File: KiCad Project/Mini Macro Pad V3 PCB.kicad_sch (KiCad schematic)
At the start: 98 parts, among them J1 USB_C_Receptacle_USB2.0_14P, SW1 SW_Push bootsel, SW10 SW_Push, SW11 SW_Push, SW12 SW_Push, SW13 SW_Push, SW14 SW_Push, SW15 SW_Push, SW16 SW_Push, SW17 SW_Push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

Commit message: more routing traces.
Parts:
- added R7: DNF, Resistor_SMD:R_0402_1005Metric_Pad0.72x0.64mm_HandSolder, symbol Device:R_Small
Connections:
- net +3.3V: now also R7.2; no longer R1.2, U1.56 (QSPI_SS), U3.1 (~{CS})
- new net QSPI_SS: R1.2, R7.1, U1.56 (QSPI_SS), U3.1 (~{CS})
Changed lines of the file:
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@@
 	)
 	(junction
-		(at 57.15 151.13)
+		(at 35.56 113.03)
 		(diameter 0)
 		(color 0 0 0 0)
 	)
 	(junction
-		(at 252.73 50.8)
+		(at 57.15 151.13)
 		(diameter 0)
 		(color 0 0 0 0)
 	)
 	(junction
-		(at 96.52 185.42)
+		(at 252.73 50.8)
 		(diameter 0)
 		(color 0 0 0 0)
 	)
 	(junction
-		(at 132.08 156.21)
+		(at 96.52 185.42)
 		(diameter 0)
 		(color 0 0 0 0)
 	)
 	(junction
-		(at 58.42 106.68)
+		(at 132.08 156.21)
 		(diameter 0)
 		(color 0 0 0 0)
@@
 	)
 	(junction
-		(at 35.56 19.05)
+		(at 58.42 104.14)
 		(diameter 0)
 		(color 0 0 0 0)
 	)
 	(junction
-		(at 35.56 113.03)
+		(at 35.56 19.05)
 		(diameter 0)
 		(color 0 0 0 0)
@@
 	(wire
 		(pts
+			(xy 35.56 104.14) (xy 35.56 113.03)
+		)
+		(stroke
+			(width 0)
+			(type default)
+		)
+	)
+	(wire
+		(pts
 			(xy 144.78 186.69) (xy 144.78 187.96)
 		)
@@
 	(wire
 		(pts
+			(xy 55.88 104.14) (xy 58.42 104.14)
+		)
+		(stroke
+			(width 0)
+			(type default)
+		)
+	)
+	(wire
+		(pts
 			(xy 196.85 54.61) (xy 203.2 54.61)
 		)
@@
 	(wire
 		(pts
+			(xy 35.56 113.03) (xy 48.26 113.03)
+		)
+		(stroke
+			(width 0)
+			(type default)
+		)
+	)
+	(wire
+		(pts
 			(xy 231.14 96.52) (xy 232.41 96.52)
 		)
@@
 	(wire
 		(pts
-			(xy 135.89 175.26) (xy 134.62 175.26)
-		)
-		(stroke
-			(width 0)
-			(type default)
-		)
-	)
-	(wire
-		(pts
 			(xy 231.14 73.66) (xy 246.38 73.66)
 		)
@@
 	(wire
 		(pts
-			(xy 35.56 106.68) (xy 35.56 113.03)
-		)
-		(stroke
-			(width 0)
-			(type default)
-		)
-	)
-	(wire
-		(pts
 			(xy 121.92 185.42) (xy 121.92 195.58)
 		)
@@
 	(wire
 		(pts
-			(xy 58.42 96.52) (xy 58.42 106.68)
+			(xy 58.42 96.52) (xy 58.42 104.14)
 		)
 		(stroke
@@
 	(wire
 		(pts
-			(xy 35.56 113.03) (xy 48.26 113.03)
-		)
-		(stroke
-			(width 0)
-			(type default)
-		)
-	)
-	(wire
-		(pts
 			(xy 231.14 119.38) (xy 232.41 119.38)
 		)
@@
 	(wire
 		(pts
-			(xy 97.79 185.42) (xy 96.52 185.42)
-		)
-		(stroke
-			(width 0)
-			(type default)
-		)
-	)
-	(wire
-		(pts
 			(xy 109.22 165.1) (xy 109.22 175.26)
 		)
@@
 	(wire
 		(pts
-			(xy 35.56 106.68) (xy 58.42 106.68)
+			(xy 35.56 104.14) (xy 50.8 104.14)
 		)
 		(stroke
@@
 	(wire
 		(pts
-			(xy 58.42 106.68) (xy 58.42 107.95)
+			(xy 58.42 104.14) (xy 58.42 107.95)
 		)
 		(stroke
@@
 		)
 	)
+	(label "USB_BOOTSEL"
+		(at 49.53 104.14 180)
+		(effects
+			(font
+				(size 1.27 1.27)
+			)
+			(justify right bottom)
+		)
+	)
 	(label "MATRIX_R1"
 		(at 156.21 156.21 180)
@@
 					(unit 1)
 				)
+			)
+		)
+	)
+	(symbol
+		(lib_id "Device:R_Small")
+		(at 53.34 104.14 90)
+		(unit 1)
+		(exclude_from_sim yes)
+		(in_bom no)
+		(on_board no)
+		(dnp yes)
+		(fields_autoplaced yes)
+		(property "Reference" "R7"
+			(at 53.34 99.06 90)
+			(effects
+				(font
+					(size 1.016 1.016)
+				)
+			)
+		)
+		(property "Value" "DNF"
+			(at 53.34 101.6 90)
+			(effects
+				(font
+					(size 1.27 1.27)
+				)
+			)
+		)
+		(property "Footprint" "Resistor_SMD:R_0402_1005Metric_Pad0.72x0.64mm_HandSolder"
+			(at 53.34 104.14 0)
+			(effects
+				(font
+					(size 1.27 1.27)
+				)
+				(hide yes)
+			)
+		)
+		(property "Datasheet" "~"
+			(at 53.34 104.14 0)
+			(effects
+				(font
+					(size 1.27 1.27)
+				)
+				(hide yes)
+			)
+		)
+		(property "Description" "Resistor, small symbol"
+			(at 53.34 104.14 0)
+			(effects
+				(font
+					(size 1.27 1.27)
+				)
+				(hide yes)
+			)
+		)
+		(pin "1"
+		)
+		(pin "2"
+		)
+		(instances
+			(project "Mini Macro Pad V3 PCB"
+				(path "/2a066f6e-231b-48de-a223-e3e72af8ed07"
+					(reference "R7")
+					(unit 1)
+				)

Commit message: more routing work
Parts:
- removed TP10, TP11, TP12, TP7, TP8, TP9: ~, TestPoint:TestPoint_Pad_1.5x1.5mm, symbol Connector:TestPoint
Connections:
- net +3.3V: now also U1.26 (RUN)
- no-connect marks 2 -> 7

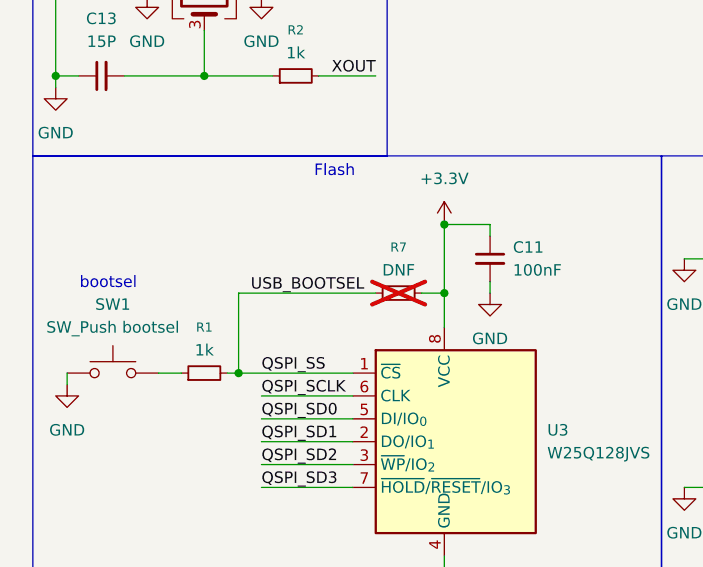
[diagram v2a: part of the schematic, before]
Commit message: tweaks for DRC
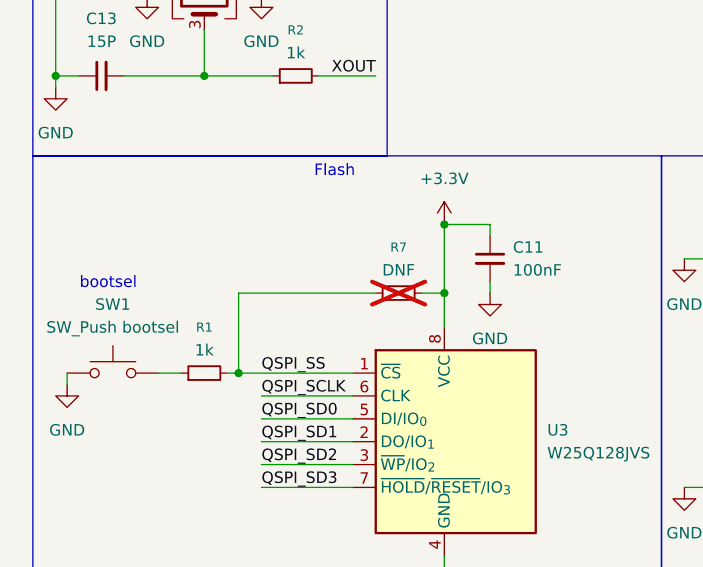
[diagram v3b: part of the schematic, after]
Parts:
- U1: footprint Package_DFN_QFN:QFN-56-1EP_7x7mm_P0.4mm_EP3.2x3.2mm -> Package_DFN_QFN:QFN-56-1EP_7x7mm_P0.4mm_EP3.2x3.2mm_ThermalVias
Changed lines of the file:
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@@
 		)
 	)
-	(label "USB_BOOTSEL"
-		(at 49.53 104.14 180)
-		(effects
-			(font
-				(size 1.27 1.27)
-			)
-			(justify right bottom)
-		)
-	)
 	(label "MATRIX_R1"
 		(at 156.21 156.21 180)
@@
 			)
 		)
-		(property "Footprint" "Package_DFN_QFN:QFN-56-1EP_7x7mm_P0.4mm_EP3.2x3.2mm"
+		(property "Footprint" "Package_DFN_QFN:QFN-56-1EP_7x7mm_P0.4mm_EP3.2x3.2mm_ThermalVias"
 			(at 205.74 109.22 0)
 			(effects

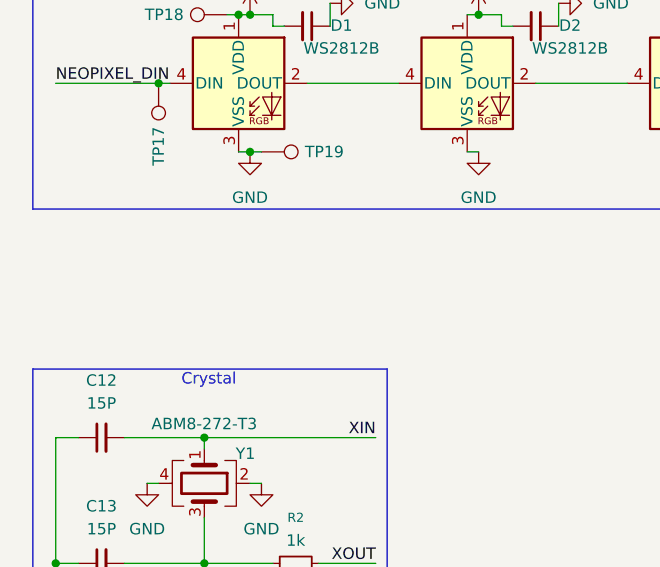
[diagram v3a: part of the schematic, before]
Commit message: added silkscreen things
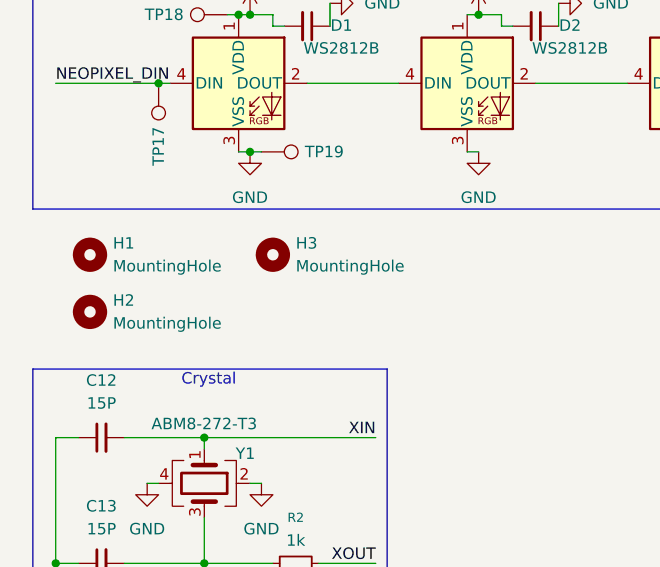
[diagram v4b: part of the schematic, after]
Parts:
- added H1, H2, H3: MountingHole, MountingHole:ToolingHole_1.152mm, symbol Mechanical:MountingHole
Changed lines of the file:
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@@
 	)
 	(symbol
+		(lib_id "Mechanical:MountingHole")
+		(at 39.37 45.72 0)
+		(unit 1)
+		(exclude_from_sim no)
+		(in_bom no)
+		(on_board yes)
+		(dnp no)
+		(fields_autoplaced yes)
+		(property "Reference" "H3"
+			(at 41.91 44.4499 0)
+			(effects
+				(font
+					(size 1.27 1.27)
+				)
+				(justify left)
+			)
+		)
+		(property "Value" "MountingHole"
+			(at 41.91 46.9899 0)
+			(effects
+				(font
+					(size 1.27 1.27)
+				)
+				(justify left)
+			)
+		)
+		(property "Footprint" "MountingHole:ToolingHole_1.152mm"
+			(at 39.37 45.72 0)
+			(effects
+				(font
+					(size 1.27 1.27)
+				)
+				(hide yes)
+			)
+		)
+		(property "Datasheet" "~"
+			(at 39.37 45.72 0)
+			(effects
+				(font
+					(size 1.27 1.27)
+				)
+				(hide yes)
+			)
+		)
+		(property "Description" "Mounting Hole without connection"
+			(at 39.37 45.72 0)
+			(effects
+				(font
+					(size 1.27 1.27)
+				)
+				(hide yes)
+			)
+		)
+		(instances
+			(project ""
+				(path "/2a066f6e-231b-48de-a223-e3e72af8ed07"
+					(reference "H3")
+					(unit 1)
+				)
+			)
+		)
+	)
+	(symbol
 		(lib_id "Device:C")
 		(at 83.82 156.21 0)
@@
 					(unit 1)
 				)
+			)
+		)
+	)
+	(symbol
+		(lib_id "Mechanical:MountingHole")
+		(at 19.05 45.72 0)
+		(unit 1)
+		(exclude_from_sim no)
+		(in_bom no)
+		(on_board yes)
+		(dnp no)
+		(fields_autoplaced yes)
+		(property "Reference" "H1"
+			(at 21.59 44.4499 0)
+			(effects
+				(font
+					(size 1.27 1.27)
+				)
+				(justify left)
+			)
+		)
+		(property "Value" "MountingHole"
+			(at 21.59 46.9899 0)
+			(effects
+				(font
+					(size 1.27 1.27)
+				)
+				(justify left)
+			)
+		)
+		(property "Footprint" "MountingHole:ToolingHole_1.152mm"
+			(at 19.05 45.72 0)
+			(effects
+				(font
+					(size 1.27 1.27)
+				)
+				(hide yes)
+			)
+		)
+		(property "Datasheet" "~"
+			(at 19.05 45.72 0)
+			(effects
+				(font
+					(size 1.27 1.27)
+				)
+				(hide yes)
+			)
+		)
+		(property "Description" "Mounting Hole without connection"
+			(at 19.05 45.72 0)
+			(effects
+				(font
+					(size 1.27 1.27)
+				)
+				(hide yes)
+			)
+		)
+		(instances
+			(project ""
+				(path "/2a066f6e-231b-48de-a223-e3e72af8ed07"
+					(reference "H1")
+					(unit 1)
+				)
+			)
+		)
+	)
+	(symbol
+		(lib_id "Mechanical:MountingHole")
+		(at 19.05 52.07 0)
+		(unit 1)
+		(exclude_from_sim no)
+		(in_bom no)
+		(on_board yes)
+		(dnp no)
+		(fields_autoplaced yes)
+		(property "Reference" "H2"
+			(at 21.59 50.7999 0)
+			(effects
+				(font
+					(size 1.27 1.27)
+				)
+				(justify left)
+			)
+		)
+		(property "Value" "MountingHole"
+			(at 21.59 53.3399 0)
+			(effects
+				(font
+					(size 1.27 1.27)
+				)
+				(justify left)
+			)
+		)
+		(property "Footprint" "MountingHole:ToolingHole_1.152mm"
+			(at 19.05 52.07 0)
+			(effects
+				(font
+					(size 1.27 1.27)
+				)
+				(hide yes)
+			)
+		)
+		(property "Datasheet" "~"
+			(at 19.05 52.07 0)
+			(effects
+				(font
+					(size 1.27 1.27)
+				)
+				(hide yes)
+			)
+		)
+		(property "Description" "Mounting Hole without connection"
+			(at 19.05 52.07 0)
+			(effects
+				(font
+					(size 1.27 1.27)
+				)
+				(hide yes)
+			)
+		)
+		(instances
+			(project ""
+				(path "/2a066f6e-231b-48de-a223-e3e72af8ed07"
+					(reference "H2")
+					(unit 1)
+				)

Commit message: small tweaks before ordering first prototype
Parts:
- added TP7, TP8: ~, TestPoint:TestPoint_Pad_1.5x1.5mm, symbol Connector:TestPoint
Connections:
- net USB_D+: now also TP8.1
- net USB_D-: now also TP7.1
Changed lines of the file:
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@@
+	)
+	(symbol
+		(lib_id "Connector:TestPoint")
+		(at 54.61 171.45 270)
+		(unit 1)
+		(exclude_from_sim no)
+		(in_bom yes)
+		(on_board yes)
+		(dnp no)
+		(property "Reference" "TP8"
+			(at 59.436 171.45 90)
+			(effects
+				(font
+					(size 1.27 1.27)
+				)
+				(justify left)
+			)
+		)
+		(property "Value" "~"
+			(at 59.69 172.7199 90)
+			(effects
+				(font
+					(size 1.27 1.27)
+				)
+				(justify left)
+				(hide yes)
+			)
+		)
+		(property "Footprint" "TestPoint:TestPoint_Pad_1.5x1.5mm"
+			(at 54.61 176.53 0)
+			(effects
+				(font
+					(size 1.27 1.27)
+				)
+				(hide yes)
+			)
+		)
+		(property "Datasheet" "~"
+			(at 54.61 176.53 0)
+			(effects
+				(font
+					(size 1.27 1.27)
+				)
+				(hide yes)
+			)
+		)
+		(property "Description" "test point"
+			(at 54.61 171.45 0)
+			(effects
+				(font
+					(size 1.27 1.27)
+				)
+				(hide yes)
+			)
+		)
+		(pin "1"
+		)
+		(instances
+			(project "Mini Macro Pad V3 PCB"
+				(path "/2a066f6e-231b-48de-a223-e3e72af8ed07"
+					(reference "TP8")
+					(unit 1)
+				)
+			)
+		)
 	)
 	(symbol
@@
 					(unit 1)
 				)
+			)
+		)
+	)
+	(symbol
+		(lib_id "Connector:TestPoint")
+		(at 54.61 167.64 270)
+		(unit 1)
+		(exclude_from_sim no)
+		(in_bom yes)
+		(on_board yes)
+		(dnp no)
+		(property "Reference" "TP7"
+			(at 59.436 167.64 90)
+			(effects
+				(font
+					(size 1.27 1.27)
+				)
+				(justify left)
+			)
+		)
+		(property "Value" "~"
+			(at 59.69 168.9099 90)
+			(effects
+				(font
+					(size 1.27 1.27)
+				)
+				(justify left)
+				(hide yes)
+			)
+		)
+		(property "Footprint" "TestPoint:TestPoint_Pad_1.5x1.5mm"
+			(at 54.61 172.72 0)
+			(effects
+				(font
+					(size 1.27 1.27)
+				)
+				(hide yes)
+			)
+		)
+		(property "Datasheet" "~"
+			(at 54.61 172.72 0)
+			(effects
+				(font
+					(size 1.27 1.27)
+				)
+				(hide yes)
+			)
+		)
+		(property "Description" "test point"
+			(at 54.61 167.64 0)
+			(effects
+				(font
+					(size 1.27 1.27)
+				)
+				(hide yes)
+			)
+		)
+		(pin "1"
+		)
+		(instances
+			(project "Mini Macro Pad V3 PCB"
+				(path "/2a066f6e-231b-48de-a223-e3e72af8ed07"
+					(reference "TP7")
+					(unit 1)
+				)

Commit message: changed capacitor & resistor sizes
changed sizes from 0402 to 0603 & replaced BOOTSEL button with the same kind as all the others
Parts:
- C1, C10, C11, C12, C13, C14, C15, C16, C17, C18, C19, C2, C20, C21, C22, C23, C3, C4, C5, C6, C7, C8, C9: footprint Capacitor_SMD:C_0402_1005Metric_Pad0.74x0.62mm_HandSolder -> Capacitor_SMD:C_0603_1608Metric
- R1, R2, R3, R4, R5, R6: footprint Resistor_SMD:R_0402_1005Metric_Pad0.72x0.64mm_HandSolder -> Resistor_SMD:R_0603_1608Metric
- SW1: footprint Button_Switch_SMD:Panasonic_EVQPUK_EVQPUB -> Button_Switch_THT:SW_PUSH_6mm_H4.3mm; LSSC (none) -> C526225
- U1: LSSC (none) -> C2040
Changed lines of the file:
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@@
 			)
 		)
-		(property "Footprint" "Capacitor_SMD:C_0402_1005Metric_Pad0.74x0.62mm_HandSolder"
+		(property "Footprint" "Capacitor_SMD:C_0603_1608Metric"
 			(at 252.73 53.34 0)
 			(effects
@@
 			)
 		)
-		(property "Footprint" "Resistor_SMD:R_0402_1005Metric_Pad0.72x0.64mm_HandSolder"
+		(property "Footprint" "Resistor_SMD:R_0603_1608Metric"
 			(at 171.45 73.66 0)
 			(effects
@@
 			)
 		)
-		(property "Footprint" "Resistor_SMD:R_0402_1005Metric_Pad0.72x0.64mm_HandSolder"
+		(property "Footprint" "Resistor_SMD:R_0603_1608Metric"
 			(at 41.91 80.01 0)
 			(effects
@@
 			)
 		)
-		(property "Footprint" "Button_Switch_SMD:Panasonic_EVQPUK_EVQPUB"
+		(property "Footprint" "Button_Switch_THT:SW_PUSH_6mm_H4.3mm"
 			(at 21.59 107.95 0)
 			(effects
@@
 			)
 		)
-		(property "Datasheet" "~"
+		(property "Datasheet" "https://jlcpcb.com/api/file/downloadByFileSystemAccessId/8588913898988298240"
 			(at 21.59 107.95 0)
 			(effects
@@
 			)
 		)
+		(property "LSSC" "C526225"
+			(at 21.59 113.03 0)
+			(effects
+				(font
+					(size 1.27 1.27)
+				)
+				(hide yes)
+			)
+		)
 		(pin "2"
 		)
@@
 			)
 		)
-		(property "Footprint" "Resistor_SMD:R_0402_1005Metric_Pad0.72x0.64mm_HandSolder"
+		(property "Footprint" "Resistor_SMD:R_0603_1608Metric"
 			(at 46.99 158.75 0)
 			(effects
@@
 			)
 		)
-		(property "Footprint" "Resistor_SMD:R_0402_1005Metric_Pad0.72x0.64mm_HandSolder"
+		(property "Footprint" "Resistor_SMD:R_0603_1608Metric"
 			(at 171.45 81.28 0)
 			(effects
@@
 			)
 		)
-		(property "Footprint" "Capacitor_SMD:C_0402_1005Metric_Pad0.74x0.62mm_HandSolder"
+		(property "Footprint" "Capacitor_SMD:C_0603_1608Metric"
 			(at 84.7852 160.02 0)
 			(effects
@@
 			)
 		)
-		(property "Footprint" "Capacitor_SMD:C_0402_1005Metric_Pad0.74x0.62mm_HandSolder"
+		(property "Footprint" "Capacitor_SMD:C_0603_1608Metric"
 			(at 275.59 53.34 0)
 			(effects
@@
 			)
 		)
-		(property "Footprint" "Resistor_SMD:R_0402_1005Metric_Pad0.72x0.64mm_HandSolder"
+		(property "Footprint" "Resistor_SMD:R_0603_1608Metric"
 			(at 31.75 113.03 0)
 			(effects
@@
 			)
 		)
-		(property "Footprint" "Capacitor_SMD:C_0402_1005Metric_Pad0.74x0.62mm_HandSolder"
+		(property "Footprint" "Capacitor_SMD:C_0603_1608Metric"
 			(at 58.1152 160.02 0)
 			(effects
@@
 			)
 		)
-		(property "Footprint" "Resistor_SMD:R_0402_1005Metric_Pad0.72x0.64mm_HandSolder"
+		(property "Footprint" "Resistor_SMD:R_0603_1608Metric"
 			(at 46.99 156.21 0)
 			(effects
@@
 			)
 		)
-		(property "Footprint" "Capacitor_SMD:C_0402_1005Metric_Pad0.74x0.62mm_HandSolder"
+		(property "Footprint" "Capacitor_SMD:C_0603_1608Metric"
 			(at 43.18 20.32 0)
 			(effects
@@
 			)
 		)
-		(property "Footprint" "Capacitor_SMD:C_0402_1005Metric_Pad0.74x0.62mm_HandSolder"
+		(property "Footprint" "Capacitor_SMD:C_0603_1608Metric"
 			(at 241.3 53.34 0)
 			(effects
@@
 			)
 		)
-		(property "Footprint" "Capacitor_SMD:C_0402_1005Metric_Pad0.74x0.62mm_HandSolder"
+		(property "Footprint" "Capacitor_SMD:C_0603_1608Metric"
 			(at 20.32 80.01 0)
 			(effects
@@
 			)
 		)
-		(property "Footprint" "Capacitor_SMD:C_0402_1005Metric_Pad0.74x0.62mm_HandSolder"
+		(property "Footprint" "Capacitor_SMD:C_0603_1608Metric"
 			(at 144.78 20.32 0)
 			(effects
@@
 			)
 		)
-		(property "Footprint" "Capacitor_SMD:C_0402_1005Metric_Pad0.74x0.62mm_HandSolder"
+		(property "Footprint" "Capacitor_SMD:C_0603_1608Metric"
 			(at 68.58 20.32 0)
 			(effects
@@
 			)
 		)
-		(property "Footprint" "Capacitor_SMD:C_0402_1005Metric_Pad0.74x0.62mm_HandSolder"
+		(property "Footprint" "Capacitor_SMD:C_0603_1608Metric"
 			(at 195.58 20.32 0)
 			(effects
@@
 			)
 		)
-		(property "Footprint" "Capacitor_SMD:C_0402_1005Metric_Pad0.74x0.62mm_HandSolder"
+		(property "Footprint" "Capacitor_SMD:C_0603_1608Metric"
 			(at 229.87 53.34 0)
 			(effects
@@
 			)
 		)
-		(property "Footprint" "Capacitor_SMD:C_0402_1005Metric_Pad0.74x0.62mm_HandSolder"
+		(property "Footprint" "Capacitor_SMD:C_0603_1608Metric"
 			(at 63.5 100.33 0)
 			(effects
@@
 			)
 		)
-		(property "Footprint" "Capacitor_SMD:C_0402_1005Metric_Pad0.74x0.62mm_HandSolder"
+		(property "Footprint" "Capacitor_SMD:C_0603_1608Metric"
 			(at 93.98 20.32 0)
 			(effects
@@
 			)
 		)
-		(property "Footprint" "Capacitor_SMD:C_0402_1005Metric_Pad0.74x0.62mm_HandSolder"
+		(property "Footprint" "Capacitor_SMD:C_0603_1608Metric"
 			(at 218.44 53.34 0)
 			(effects
@@
 			)
 		)
-		(property "Footprint" "Capacitor_SMD:C_0402_1005Metric_Pad0.74x0.62mm_HandSolder"
+		(property "Footprint" "Capacitor_SMD:C_0603_1608Metric"
 			(at 20.32 66.04 0)
 			(effects
@@
 			)
 		)
-		(property "Footprint" "Capacitor_SMD:C_0402_1005Metric_Pad0.74x0.62mm_HandSolder"
+		(property "Footprint" "Capacitor_SMD:C_0603_1608Metric"
 			(at 220.98 20.32 0)
 			(effects
@@
 			)
 		)
-		(property "Footprint" "Capacitor_SMD:C_0402_1005Metric_Pad0.74x0.62mm_HandSolder"
+		(property "Footprint" "Capacitor_SMD:C_0603_1608Metric"
 			(at 215.9 60.96 0)
 			(effects
@@
 			)
 		)
-		(property "Footprint" "Capacitor_SMD:C_0402_1005Metric_Pad0.74x0.62mm_HandSolder"
+		(property "Footprint" "Capacitor_SMD:C_0603_1608Metric"
 			(at 270.51 20.32 0)
 			(effects
@@
 			)
 		)
+		(property "LSSC" "C2040"
+			(at 205.74 109.22 0)
+			(effects
+				(font
+					(size 1.27 1.27)
+				)
+				(hide yes)
+			)
+		)
 		(pin "50"
 		)
@@
 			)
 		)
-		(property "Footprint" "Capacitor_SMD:C_0402_1005Metric_Pad0.74x0.62mm_HandSolder"
+		(property "Footprint" "Capacitor_SMD:C_0603_1608Metric"
 			(at 246.38 20.32 0)
 			(effects
@@
 			)
 		)
-		(property "Footprint" "Capacitor_SMD:C_0402_1005Metric_Pad0.74x0.62mm_HandSolder"
+		(property "Footprint" "Capacitor_SMD:C_0603_1608Metric"
 			(at 119.38 20.32 0)
 			(effects
@@
 			)
 		)
-		(property "Footprint" "Capacitor_SMD:C_0402_1005Metric_Pad0.74x0.62mm_HandSolder"
+		(property "Footprint" "Capacitor_SMD:C_0603_1608Metric"
 			(at 264.16 53.34 0)
 			(effects
@@
 			)
 		)
-		(property "Footprint" "Capacitor_SMD:C_0402_1005Metric_Pad0.74x0.62mm_HandSolder"
+		(property "Footprint" "Capacitor_SMD:C_0603_1608Metric"
 			(at 170.18 20.32 0)
 			(effects
@@
 			)
 		)
-		(property "Footprint" "Capacitor_SMD:C_0402_1005Metric_Pad0.74x0.62mm_HandSolder"
+		(property "Footprint" "Capacitor_SMD:C_0603_1608Metric"
 			(at 196.85 59.69 0)
 			(effects
